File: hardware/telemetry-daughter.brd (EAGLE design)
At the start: 65 x 56 mm, 19 parts, among them J1 GPS1, J2 MICRO-SD_CARD_SOCKET, J3 IO, J6 SMA_EDGE, U2 9DoF IMU

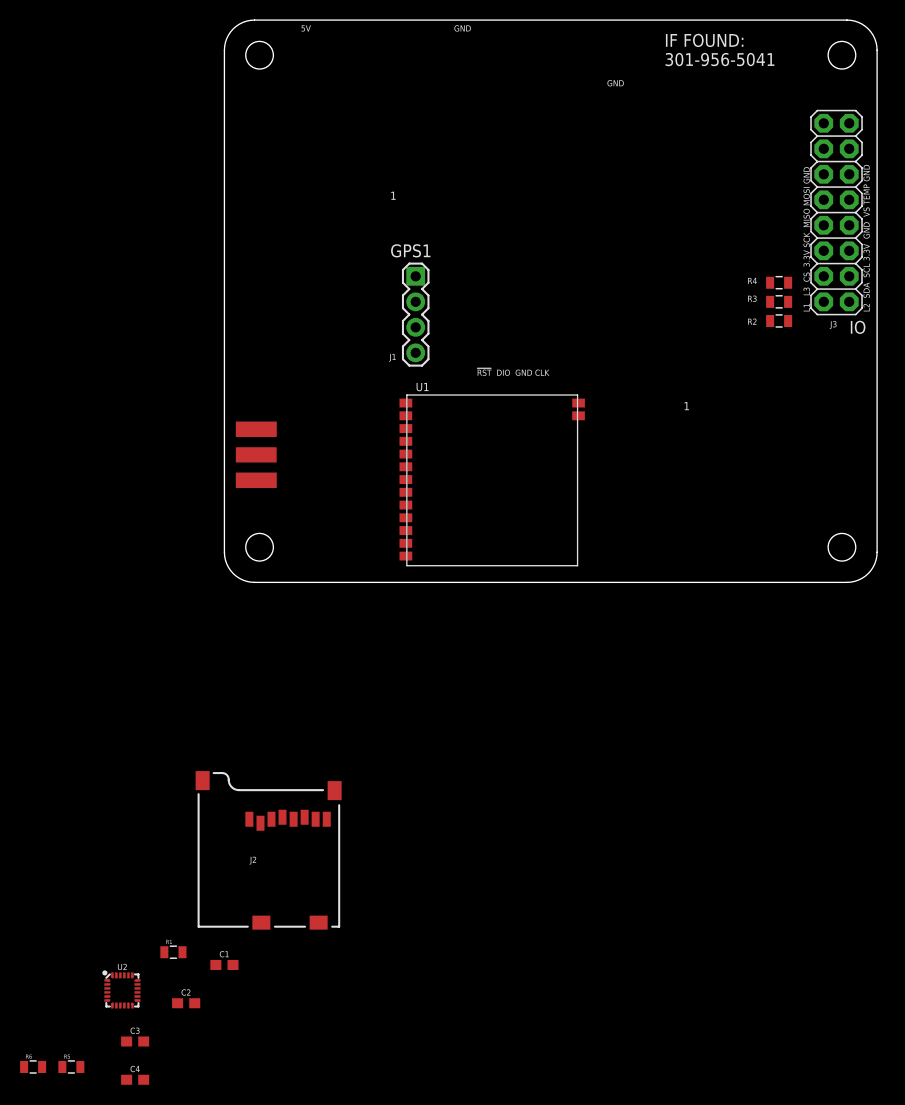
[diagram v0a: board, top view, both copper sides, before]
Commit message: Update telemetry daughter board, a few nets left to route, need to check connector placement and sizing
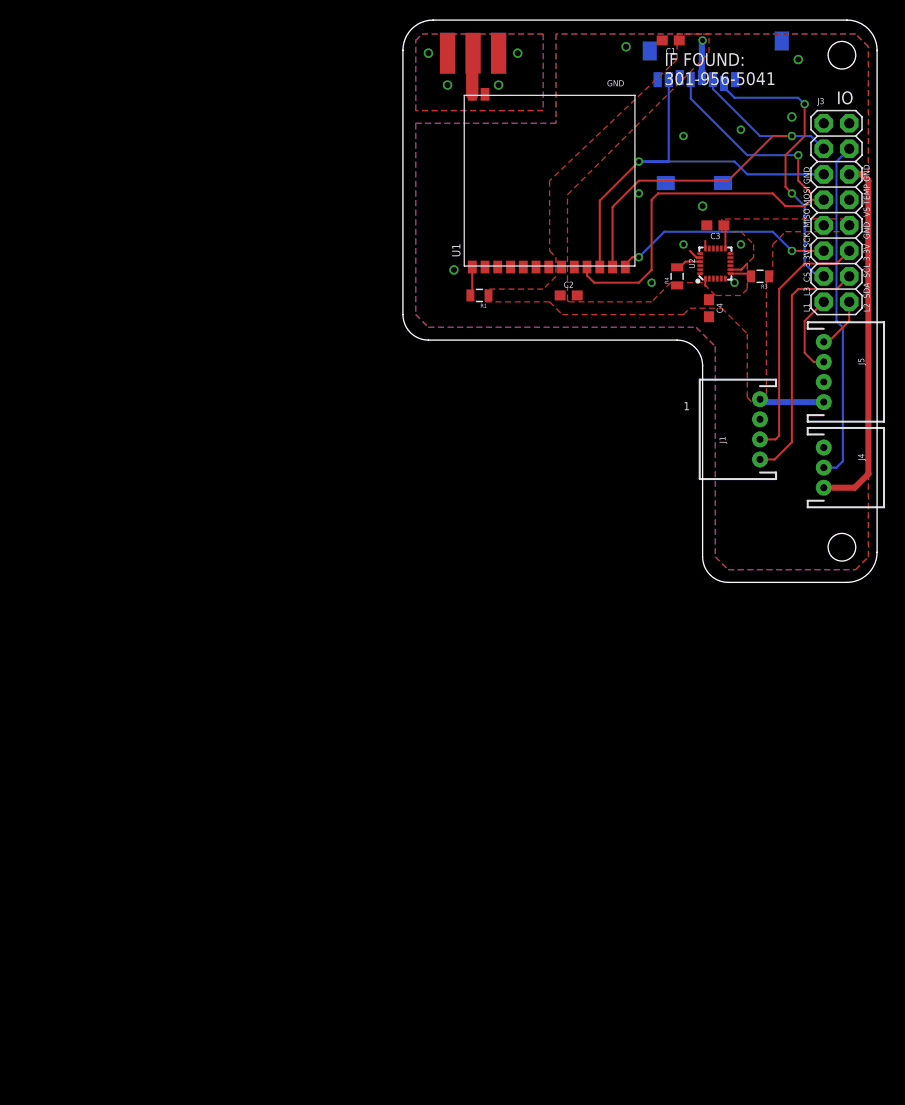
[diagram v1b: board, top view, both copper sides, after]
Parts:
- removed R2: 100, SparkFun-Passives:0805
- removed R5, R6: 10K, SparkFun-Passives:0805
- added J4: TEMP, SparkFun-Connectors:JST-3-PTH
- added J5: GPS1, SparkFun-Connectors:JST-4-PTH
- J1: value GPS1 -> I2C; device SparkFun-Connectors:1X04 -> SparkFun-Connectors:JST-4-PTH
- R3, R4: value 100 -> 10K
- U2: value 9DoF IMU -> DNP
- moved C1 102.2 mm to (44.5, 54.0), turned to 180 degrees
- moved C3 99.7 mm to (48.9, 35.6), turned to 180 degrees
- moved C4 95.8 mm to (48.3, 27.3), turned to 270 degrees
- moved U2 93.4 mm to (48.9, 31.8), turned to 90 degrees
- moved C2 80.1 mm to (34.3, 28.6)
- moved J2 79.7 mm to (41.9, 39.4), flipped to the bottom
- moved R1 72.2 mm to (25.4, 28.6), turned to 180 degrees
- moved J6 48.9 mm to (27.3, 52.7), turned to 180 degrees
- moved J1 37.5 mm to (53.3, 15.2), turned to 90 degrees
- moved U1 30.4 mm to (32.4, 40.0), turned to 90 degrees
- moved U$1 16.6 mm to (34.9, 44.5)
- moved U$2 16.3 mm to (36.8, 34.9)
- moved R4 10.2 mm to (45.1, 30.5), turned to 90 degrees
- moved R3 3.17 mm to (53.3, 30.5)
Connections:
- removed net L1: J3.2, R2.1
- removed net L2: J3.1, R3.1
- removed net L3: J3.4, R4.1
- removed net LED1: R2.2
- removed net LED2: R3.2
- removed net LED3: R4.2
- net !SD_CS!: now also J3.4
- net 3.3V: now also J5.4, R3.1, R4.1; no longer R5.1, R6.1
- net AUX_CL: now also R3.2; no longer R5.2
- net AUX_DA: now also R4.2; no longer R6.2
- net GND: now also J4.1, J5.3
- net GPSRX: now also J3.2, J5.2; no longer J1.2
- net GPSTX: now also J3.1, J5.1; no longer J1.1
- net SCL: now also J1.2
- net SDA: now also J1.1
- net TEMP: now also J4.2
- net VS: now also J4.3
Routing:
- net SCK: track 0.00 -> 53.2 mm, vias 0 -> 1
- net MISO: track 0.00 -> 42.2 mm, vias 0 -> 1
- net MOSI: track 0.00 -> 41.2 mm, vias 0 -> 1
- net VS: track 0.00 -> 36.4 mm
- net TEMP: track 0.00 -> 34.1 mm
- net !SD_CS!: track 0.00 -> 29.0 mm, vias 0 -> 2
- net SCL: track 0.00 -> 25.2 mm
- net SDA: track 0.00 -> 25.0 mm
- net !LORA_CS!: track 0.00 -> 22.2 mm, vias 0 -> 2
- net 3.3V: track 0.00 -> 15.2 mm, vias 0 -> 1
- net GPSRX: track 0.00 -> 8.15 mm
- net GPSTX: track 0.00 -> 5.31 mm
- net RF_LORA: track 0.00 -> 4.13 mm
- net !LORA_RST!: track 0.00 -> 2.91 mm
- net AUX_DA: track 0.00 -> 2.55 mm
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- added copper zone on layer 1, net 3.3V
- added copper zone on layer 1, net GND
- added copper zone on layer 16, net GND
- added copper zone on layer 1, net RGND
- added copper zone on layer 16, net RGND
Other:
- board size 65 x 56 mm -> 47.2 x 56 mm
- board text removed: "!RST! DIO GND CLK"
- board text removed: "5V"

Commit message: Connect CS and AD0 pins on the MPU9250. Fix a few small routing issues near the connector.
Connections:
- net GND: now also U2.22, U2.9
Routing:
- net GND: track 2.04 -> 4.32 mm
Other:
- board text removed: "GND"
- board text removed: "Make it your pastime Make it your mission Go ECE!"

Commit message: Route final two nets for daughtercard
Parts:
- moved U$1 12.8 mm to (47.6, 43.2), flipped to the top
- moved R4 0.90 mm to (44.5, 29.8)
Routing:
- net SCL: track 25.2 -> 39.0 mm, vias 0 -> 2
- net SDA: track 25.0 -> 38.1 mm, vias 0 -> 2
- net AUX_DA: track 2.55 -> 4.03 mm
- net GND: track 4.32 -> 3.10 mm
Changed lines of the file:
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@@
 <attribute name="VALUE" x="60.96" y="47.625" size="1.27" layer="21"/>
 </element>
-<element name="U$1" library="HAB" package="GARAGE" value="" x="34.925" y="44.45" rot="MR0"/>
+<element name="U$1" library="HAB" package="GARAGE" value="" x="47.625" y="43.18"/>
 <element name="U$2" library="HAB" package="MSFT_LOGO" value="" x="36.83" y="34.925" rot="MR0"/>
 <element name="U1" library="HAB" package="DRF1278F" value="" x="32.385" y="40.005" smashed="yes" rot="R90">
@@
 <attribute name="VALUE" x="54.356" y="31.877" size="0.4064" layer="27" rot="R180"/>
 </element>
-<element name="R4" library="SparkFun-Passives" package="0805" value="10K" x="45.085" y="30.48" smashed="yes" rot="R90">
-<attribute name="NAME" x="44.323" y="28.1305" size="0.8128" layer="25" ratio="15"/>
-<attribute name="VALUE" x="46.482" y="29.464" size="0.4064" layer="27" rot="R90"/>
+<element name="R4" library="SparkFun-Passives" package="0805" value="10K" x="44.45" y="29.845" smashed="yes" rot="R90">
+<attribute name="NAME" x="43.688" y="27.4955" size="0.8128" layer="25" ratio="15"/>
+<attribute name="VALUE" x="45.847" y="28.829" size="0.4064" layer="27" rot="R90"/>
 </element>
 <element name="J4" library="SparkFun-Connectors" package="JST-3-PTH" value="TEMP" x="59.69" y="11.43" smashed="yes" rot="R270">
@@
 <via x="45.72" y="33.655" extent="1-16" drill="0.5"/>
 <via x="41.275" y="38.735" extent="1-16" drill="0.5"/>
-<via x="45.72" y="44.45" extent="1-16" drill="0.5"/>
-<via x="51.435" y="45.085" extent="1-16" drill="0.5"/>
+<via x="45.085" y="48.26" extent="1-16" drill="0.5"/>
+<via x="52.705" y="43.815" extent="1-16" drill="0.5"/>
 <via x="56.515" y="46.355" extent="1-16" drill="0.6"/>
 <contactref element="U2" pad="22"/>
@@
 <wire x1="50.395" y1="31.55" x2="51.2572" y2="31.55" width="0.2032" layer="1"/>
 <wire x1="51.2572" y1="31.55" x2="51.2572" y2="31.75" width="0.2032" layer="1"/>
-<wire x1="47.395" y1="31.55" x2="46.79" y2="31.55" width="0.2032" layer="1"/>
-<wire x1="46.79" y1="31.55" x2="46.355" y2="31.115" width="0.2032" layer="1"/>
+<polygon width="0.1524" layer="1" orphans="yes" thermals="no">
+<vertex x="47.625" y="33.02"/>
+<vertex x="47.625" y="30.48"/>
+<vertex x="50.165" y="30.48"/>
+<vertex x="50.165" y="33.02"/>
+</polygon>
 </signal>
 <signal name="SCL">
@@
 <wire x1="62.23" y1="33.02" x2="60.96" y2="31.75" width="0.2032" layer="1"/>
 <wire x1="60.96" y1="31.75" x2="57.785" y2="31.75" width="0.2032" layer="1"/>
-<wire x1="57.785" y1="31.75" x2="55.245" y2="29.21" width="0.2032" layer="1"/>
+<wire x1="57.785" y1="31.75" x2="56.515" y2="30.48" width="0.2032" layer="1"/>
+<wire x1="56.515" y1="30.48" x2="55.245" y2="29.21" width="0.2032" layer="1"/>
 <wire x1="55.245" y1="29.21" x2="55.245" y2="14.605" width="0.2032" layer="1"/>
 <wire x1="53.34" y1="14.24" x2="54.88" y2="14.24" width="0.2032" layer="1"/>
 <wire x1="54.88" y1="14.24" x2="55.245" y2="14.605" width="0.2032" layer="1"/>
-<wire x1="55.245" y1="29.21" x2="47.395" y2="31.15" width="0" layer="19" extent="1-1"/>
+<wire x1="47.395" y1="31.15" x2="45.755" y2="31.15" width="0.2032" layer="1"/>
+<wire x1="45.755" y1="31.15" x2="45.72" y2="31.115" width="0.2032" layer="1"/>
+<via x="45.72" y="31.115" extent="1-16" drill="0.5"/>
+<via x="56.515" y="30.48" extent="1-16" drill="0.5"/>
+<wire x1="56.515" y1="30.48" x2="55.245" y2="30.48" width="0.2032" layer="16"/>
+<wire x1="55.245" y1="30.48" x2="53.975" y2="29.21" width="0.2032" layer="16"/>
+<wire x1="53.975" y1="29.21" x2="47.625" y2="29.21" width="0.2032" layer="16"/>
+<wire x1="45.72" y1="31.115" x2="47.625" y2="29.21" width="0.2032" layer="16"/>
 </signal>
 <signal name="SDA">
@@
 <wire x1="62.23" y1="30.48" x2="60.96" y2="29.21" width="0.2032" layer="1"/>
 <wire x1="60.96" y1="29.21" x2="57.15" y2="29.21" width="0.2032" layer="1"/>
-<wire x1="57.15" y1="29.21" x2="56.515" y2="28.575" width="0.2032" layer="1"/>
-<wire x1="56.515" y1="28.575" x2="56.515" y2="13.97" width="0.2032" layer="1"/>
+<wire x1="56.515" y1="27.94" x2="56.515" y2="13.97" width="0.2032" layer="1"/>
 <wire x1="56.515" y1="13.97" x2="54.785" y2="12.24" width="0.2032" layer="1"/>
 <wire x1="53.34" y1="12.24" x2="54.785" y2="12.24" width="0.2032" layer="1"/>
-<wire x1="56.515" y1="28.575" x2="47.3425" y2="30.75" width="0" layer="19" extent="1-1"/>
+<wire x1="47.3425" y1="30.75" x2="46.625" y2="30.75" width="0.2032" layer="1"/>
+<via x="46.355" y="29.21" extent="1-16" drill="0.5"/>
+<wire x1="56.515" y1="28.575" x2="57.15" y2="29.21" width="0.2032" layer="1"/>
+<wire x1="46.355" y1="29.21" x2="46.355" y2="30.48" width="0.2032" layer="1"/>
+<wire x1="46.355" y1="30.48" x2="46.625" y2="30.75" width="0.2032" layer="1"/>
+<wire x1="46.355" y1="29.21" x2="47.625" y2="27.94" width="0.2032" layer="16"/>
+<wire x1="47.625" y1="27.94" x2="56.515" y2="27.94" width="0.2032" layer="16"/>
+<via x="56.515" y="27.94" extent="1-16" drill="0.5"/>
+<wire x1="56.515" y1="27.94" x2="56.515" y2="28.575" width="0.2032" layer="1"/>
 </signal>
 <signal name="GPSTX">
@@
 <contactref element="U2" pad="21"/>
 <contactref element="R4" pad="2"/>
-<wire x1="47.395" y1="31.95" x2="45.92" y2="31.95" width="0.2032" layer="1"/>
-<wire x1="45.085" y1="31.38" x2="45.35" y2="31.38" width="0.2032" layer="1"/>
-<wire x1="45.35" y1="31.38" x2="45.92" y2="31.95" width="0.2032" layer="1"/>
+<wire x1="47.395" y1="31.95" x2="44.65" y2="31.95" width="0.2032" layer="1"/>
+<wire x1="44.65" y1="31.95" x2="44.45" y2="31.75" width="0.2032" layer="1"/>
+<wire x1="44.45" y1="31.75" x2="44.45" y2="30.745" width="0.2032" layer="1"/>
 </signal>
 <signal name="!G_INT!">

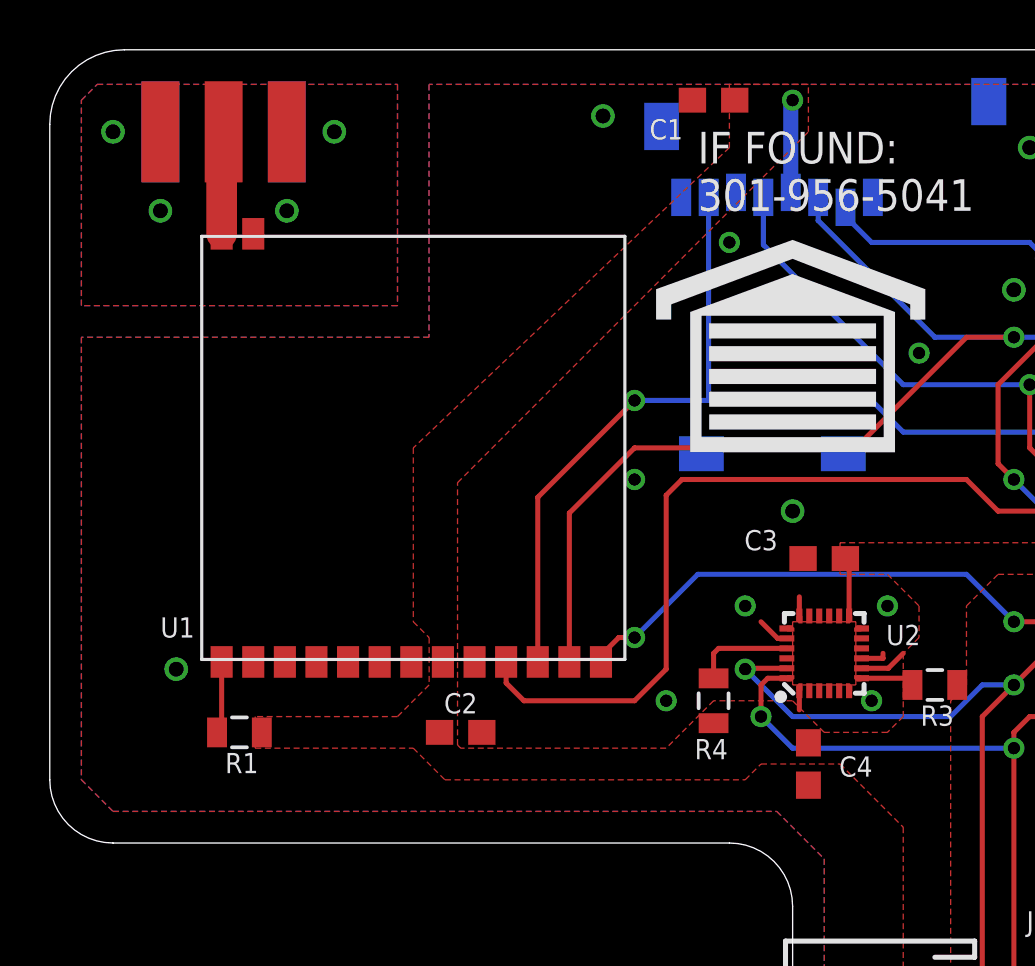
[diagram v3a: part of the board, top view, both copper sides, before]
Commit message: Change daughter card to use right angle SMA connector to remove conflict with enclosure
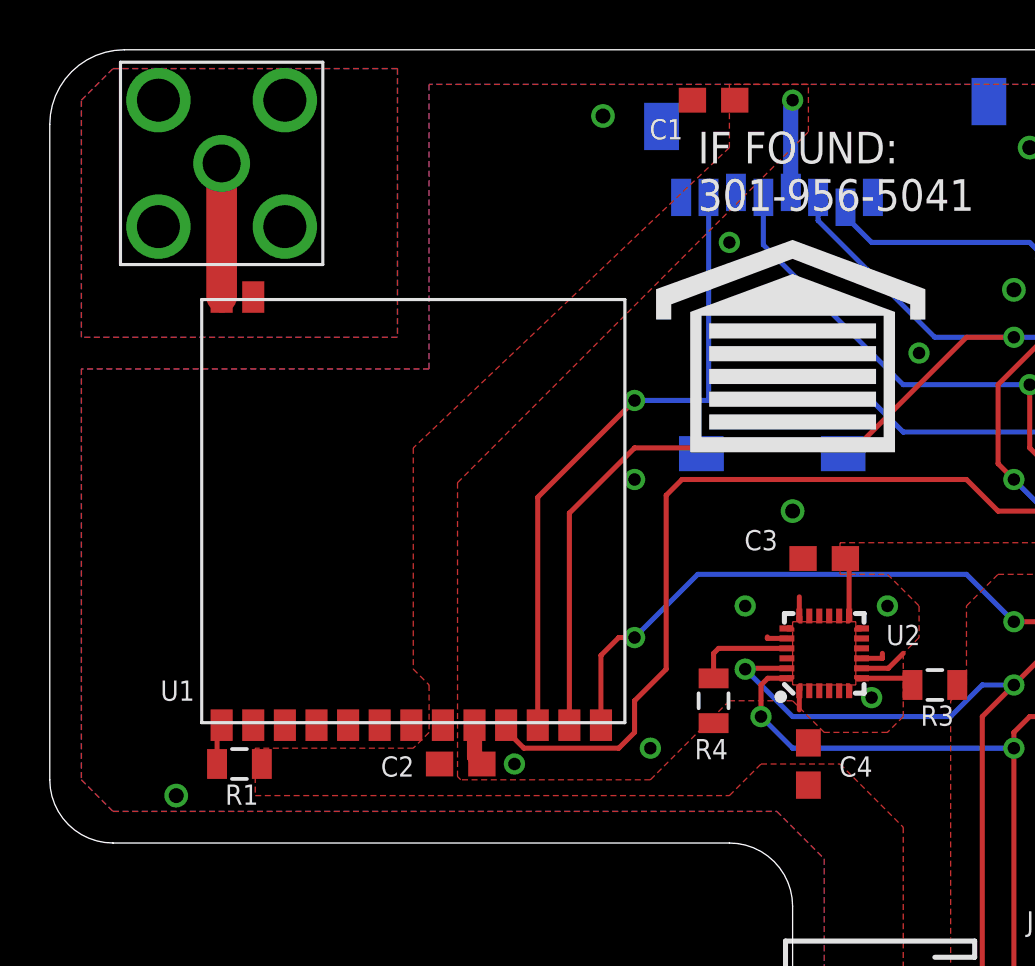
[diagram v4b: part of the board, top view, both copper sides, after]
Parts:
- removed J6: SMA_EDGE, SparkFun-Connectors:SMA-EDGE
- added U$3: SMA_VERT, HAB:SMA_VERT
- moved U1 2.54 mm to (32.4, 37.5)
- moved C2 1.27 mm to (34.3, 27.3)
- moved R1 1.27 mm to (25.4, 27.3)
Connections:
- net RF_LORA: now also U$3.P$1; no longer J6.SIG
- net RGND: now also U$3.P$2, U$3.P$3, U$3.P$4, U$3.P$5; no longer J6.GND@0, J6.GND@1, J6.GND@2, J6.GND@3
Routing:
- net MOSI: track 41.2 -> 43.7 mm
- net MISO: track 42.2 -> 44.7 mm
- net !LORA_CS!: track 22.2 -> 24.7 mm
- net RF_LORA: track 4.13 -> 5.37 mm
- net GND: track 3.10 -> 4.28 mm, vias 12 -> 13
- net !LORA_RST!: track 2.91 -> 1.74 mm
- net SCK: track 53.2 -> 54.1 mm
